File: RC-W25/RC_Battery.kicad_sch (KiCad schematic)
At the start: 18 parts, among them P2 CONN HEADER SMD R/A 2POS 2MM, SW3 SW_DPDT_x2, U2 AP62300TWU, U5 MCP73831-5-OT

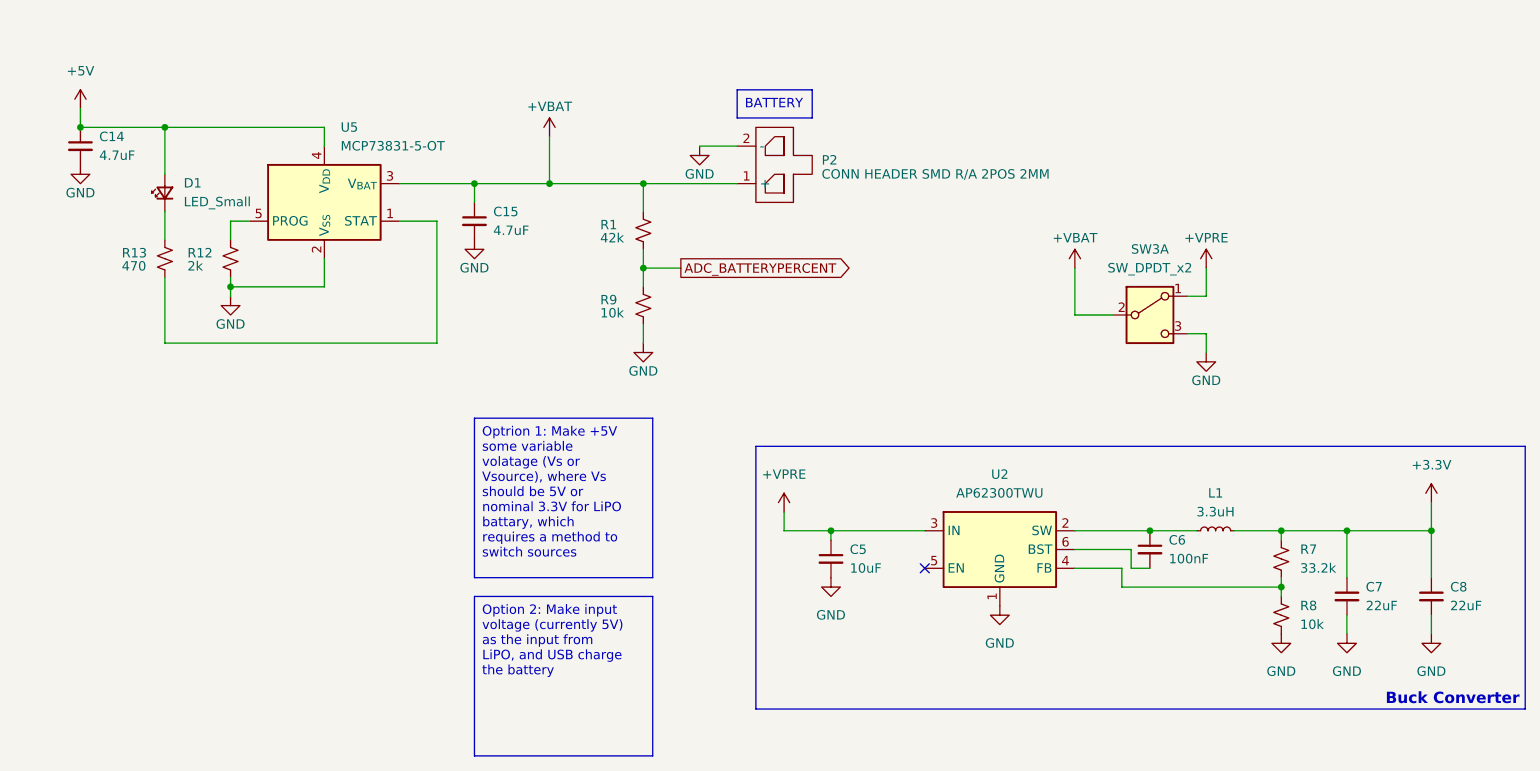
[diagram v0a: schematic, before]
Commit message: Updated Battery
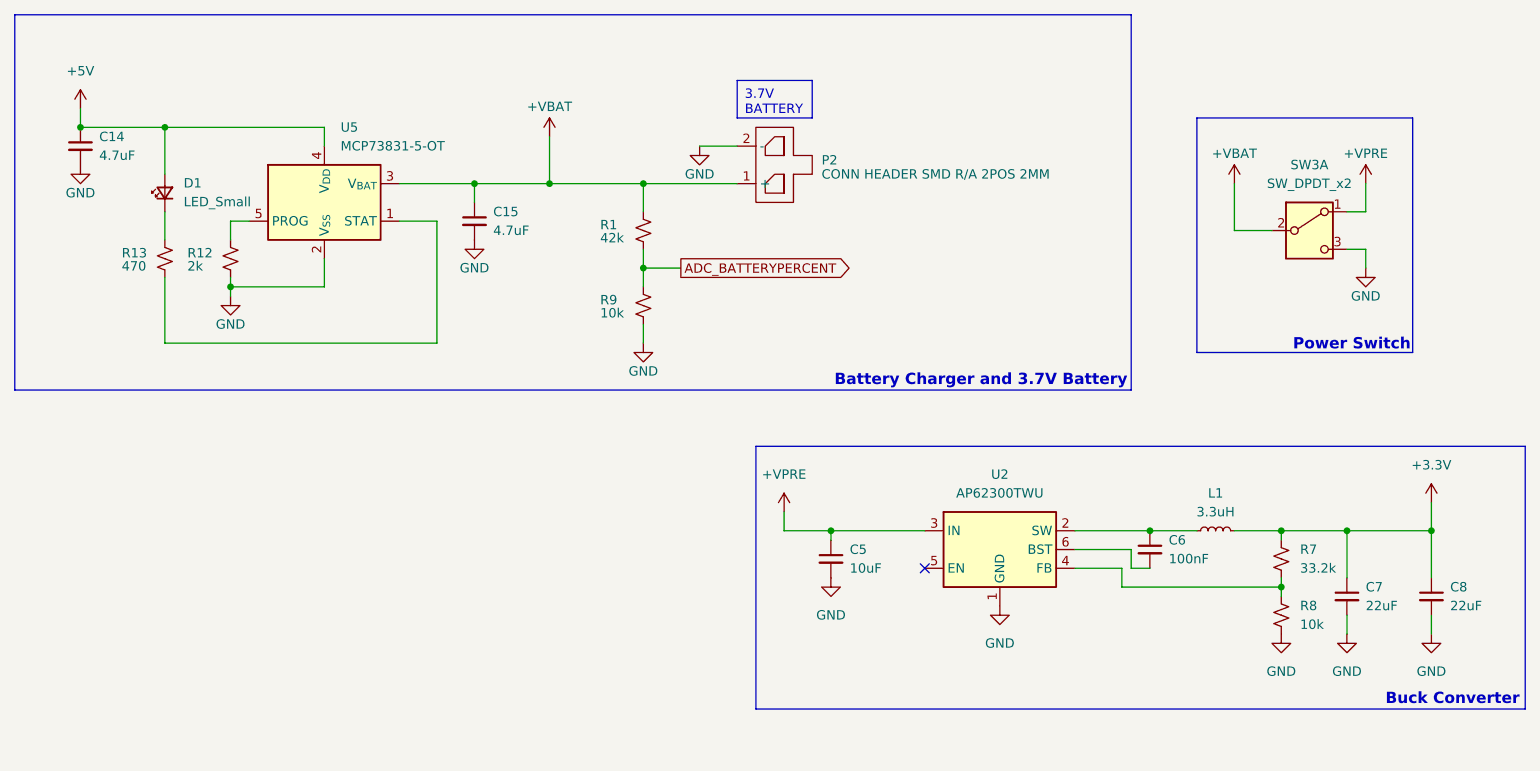
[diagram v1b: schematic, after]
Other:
- note added: "Battery Charger and 3.7V Battery"
- note added: "Power Switch"
- moved on the sheet: SW3A
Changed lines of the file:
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@@
 	(wire
 		(pts
-			(xy 204.47 81.28) (xy 204.47 85.09)
+			(xy 226.06 69.85) (xy 226.06 73.66)
 		)
 		(stroke
@@
 	(wire
 		(pts
-			(xy 186.69 81.28) (xy 186.69 87.63)
+			(xy 208.28 69.85) (xy 208.28 76.2)
 		)
 		(stroke
@@
 	(wire
 		(pts
-			(xy 204.47 92.71) (xy 204.47 90.17)
+			(xy 226.06 81.28) (xy 226.06 78.74)
 		)
 		(stroke
@@
 	(wire
 		(pts
-			(xy 201.93 85.09) (xy 204.47 85.09)
-		)
-		(stroke
-			(width 0)
-			(type default)
-		)
-	)
-	(wire
-		(pts
-			(xy 186.69 87.63) (xy 191.77 87.63)
+			(xy 223.52 73.66) (xy 226.06 73.66)
+		)
+		(stroke
+			(width 0)
+			(type default)
+		)
+	)
+	(wire
+		(pts
+			(xy 208.28 76.2) (xy 213.36 76.2)
 		)
 		(stroke
@@
 	(wire
 		(pts
-			(xy 204.47 90.17) (xy 201.93 90.17)
+			(xy 226.06 78.74) (xy 223.52 78.74)
 		)
 		(stroke
@@
 		)
 	)
-	(text_box "Option 2: Make input voltage (currently 5V) as the input from LiPO, and USB charge the battery"
-		(exclude_from_sim no)
-		(at 105.41 125.73 0)
-		(size 24.13 21.59)
+	(rectangle
+		(start 203.2 60.96)
+		(end 232.41 92.71)
 		(stroke
 			(width 0)
@@
 			(type none)
 		)
-		(effects
-			(font
-				(size 1.27 1.27)
-			)
-			(justify left top)
-		)
-	)
-	(text_box "Optrion 1: Make +5V some variable volatage (Vs or Vsource), where Vs should be 5V or nominal 3.3V for LiPO battary, which requires a method to switch sources"
-		(exclude_from_sim no)
-		(at 105.41 101.6 0)
-		(size 24.13 21.59)
+	)
+	(rectangle
+		(start 43.18 46.99)
+		(end 194.31 97.79)
 		(stroke
 			(width 0)
@@
 			(type none)
 		)
-		(effects
-			(font
-				(size 1.27 1.27)
-			)
-			(justify left top)
-		)
-	)
-	(text_box "BATTERY\n"
-		(exclude_from_sim no)
-		(at 140.97 57.15 0)
-		(size 10.16 3.81)
+	)
+	(text_box "3.7V BATTERY\n"
+		(exclude_from_sim no)
+		(at 140.97 55.88 0)
+		(size 10.16 5.08)
 		(stroke
 			(width 0)
@@
 		)
 	)
+	(text "Battery Charger and 3.7V Battery"
+		(exclude_from_sim no)
+		(at 193.802 96.52 0)
+		(effects
+			(font
+				(face "KiCad Font")
+				(size 1.524 1.524)
+				(thickness 0.3048)
+				(bold yes)
+			)
+			(justify right)
+		)
+	)
+	(text "Power Switch\n"
+		(exclude_from_sim no)
+		(at 232.156 91.694 0)
+		(effects
+			(font
+				(face "KiCad Font")
+				(size 1.524 1.524)
+				(thickness 0.3048)
+				(bold yes)
+			)
+			(justify right)
+		)
+	)
 	(global_label "ADC_BATTERYPERCENT"
 		(shape output)
@@
 	(symbol
 		(lib_id "power:+5V")
-		(at 186.69 81.28 0)
+		(at 208.28 69.85 0)
 		(unit 1)
 		(exclude_from_sim no)
@@
 		(dnp no)
 		(property "Reference" "#PWR042"
-			(at 186.69 85.09 0)
+			(at 208.28 73.66 0)
 			(effects
 				(font
@@
 		)
 		(property "Value" "+VBAT"
-			(at 186.69 77.216 0)
+			(at 208.28 65.786 0)
 			(effects
 				(font
@@
 		)
 		(property "Footprint" ""
-			(at 186.69 81.28 0)
+			(at 208.28 69.85 0)
 			(effects
 				(font
@@
 		)
 		(property "Datasheet" ""
-			(at 186.69 81.28 0)
+			(at 208.28 69.85 0)
 			(effects
 				(font
@@
 		)
 		(property "Description" "Power symbol creates a global label with name \"+5V\""
-			(at 186.69 81.28 0)
+			(at 208.28 69.85 0)
 			(effects
 				(font
@@
 	(symbol
 		(lib_id "Switch:SW_DPDT_x2")
-		(at 196.85 87.63 0)
+		(at 218.44 76.2 0)
 		(unit 1)
 		(exclude_from_sim no)
@@
 		(fields_autoplaced yes)
 		(property "Reference" "SW3"
-			(at 196.85 78.74 0)
+			(at 218.44 67.31 0)
 			(effects
 				(font
@@
 		)
 		(property "Value" "SW_DPDT_x2"
-			(at 196.85 81.28 0)
+			(at 218.44 69.85 0)
 			(effects
 				(font
@@
 		)
 		(property "Footprint" ""
-			(at 196.85 87.63 0)
+			(at 218.44 76.2 0)
 			(effects
 				(font
@@
 		)
 		(property "Datasheet" "~"
-			(at 196.85 87.63 0)
+			(at 218.44 76.2 0)
 			(effects
 				(font
@@
 		)
 		(property "Description" "Switch, dual pole double throw, separate symbols"
-			(at 196.85 87.63 0)
+			(at 218.44 76.2 0)
 			(effects
 				(font
@@
 	(symbol
 		(lib_id "power:GND")
-		(at 204.47 92.71 0)
+		(at 226.06 81.28 0)
 		(unit 1)
 		(exclude_from_sim no)
@@
 		(dnp no)
 		(property "Reference" "#PWR041"
-			(at 204.47 99.06 0)
+			(at 226.06 87.63 0)
 			(effects
 				(font
@@
 		)
 		(property "Value" "GND"
-			(at 204.47 96.52 0)
+			(at 226.06 85.09 0)
 			(effects
 				(font
@@
 		)
 		(property "Footprint" ""
-			(at 204.47 92.71 0)
+			(at 226.06 81.28 0)
 			(effects
 				(font
@@
 		)
 		(property "Datasheet" ""
-			(at 204.47 92.71 0)
+			(at 226.06 81.28 0)
 			(effects
 				(font
@@
 		)
 		(property "Description" "Power symbol creates a global label with name \"GND\" , ground"
-			(at 204.47 92.71 0)
+			(at 226.06 81.28 0)
 			(effects
 				(font
@@
 	(symbol
 		(lib_id "power:+5V")
-		(at 204.47 81.28 0)
+		(at 226.06 69.85 0)
 		(unit 1)
 		(exclude_from_sim no)
@@
 		(dnp no)
 		(property "Reference" "#PWR043"
-			(at 204.47 85.09 0)
+			(at 226.06 73.66 0)
 			(effects
 				(font
@@
 		)
 		(property "Value" "+VPRE"
-			(at 204.47 77.216 0)
+			(at 226.06 65.786 0)
 			(effects
 				(font
@@
 		)
 		(property "Footprint" ""
-			(at 204.47 81.28 0)
+			(at 226.06 69.85 0)
 			(effects
 				(font
@@
 		)
 		(property "Datasheet" ""
-			(at 204.47 81.28 0)
+			(at 226.06 69.85 0)
 			(effects
 				(font
@@
 		)
 		(property "Description" "Power symbol creates a global label with name \"+5V\""
-			(at 204.47 81.28 0)
-			(effects
-				(font
+			(at 226.06 69.85 0)
+			(effects
+				(font

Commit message: fixed resistors
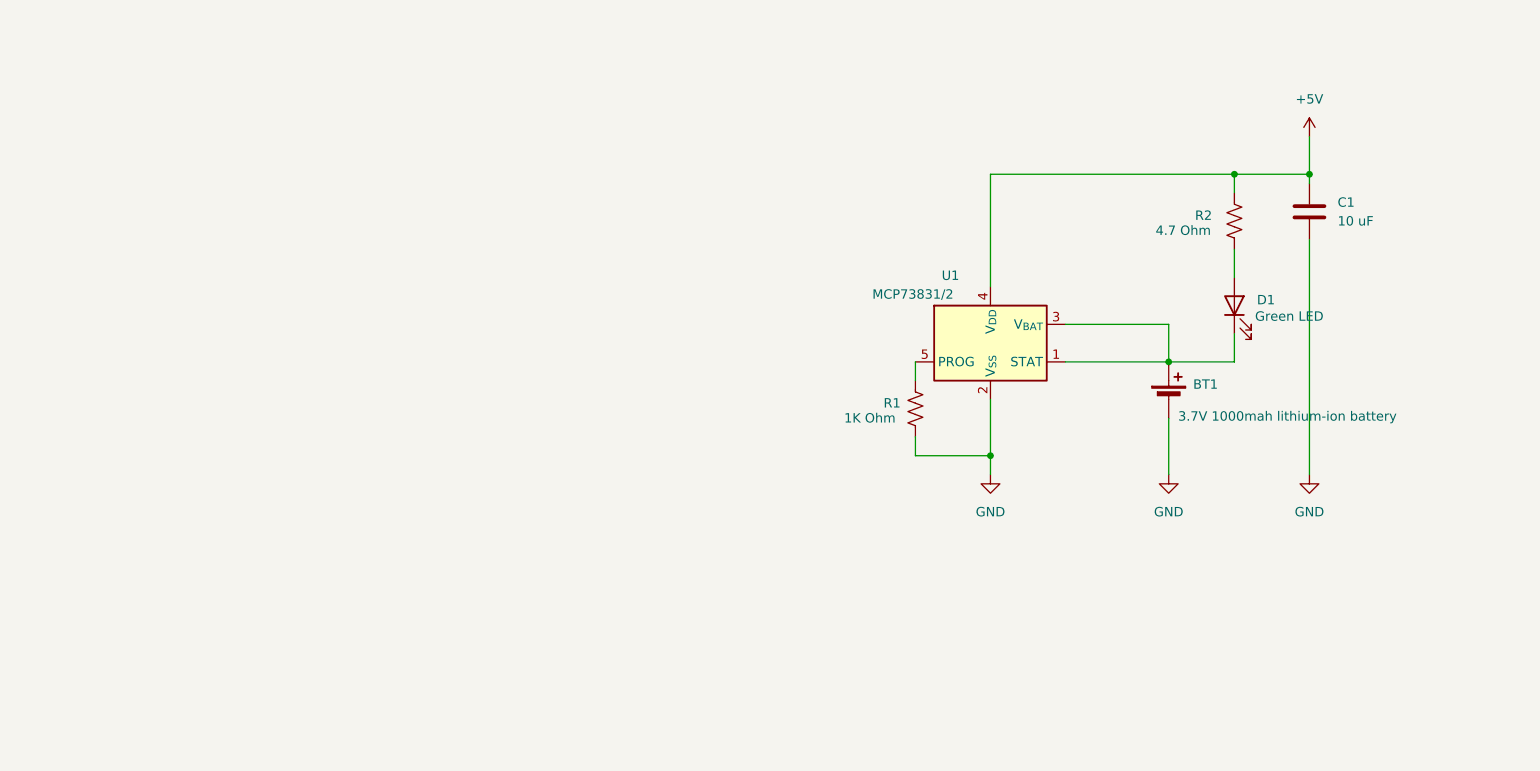
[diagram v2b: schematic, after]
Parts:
- removed C14, C15: 4.7uF, Capacitor_SMD:C_0603_1608Metric, symbol Device:C_Small
- removed C5: 10uF, Capacitor_SMD:C_0603_1608Metric, symbol Device:C_Small
- removed C6: 100nF, Capacitor_SMD:C_0603_1608Metric, symbol Device:C_Small
- removed C7, C8: 22uF, Capacitor_SMD:C_0603_1608Metric, symbol Device:C_Small
- removed D1: LED_Small, symbol Device:LED_Small
- removed L1: 3.3uH, symbol Device:L_Small
- removed P2: CONN HEADER SMD R/A 2POS 2MM, symbol New_Library:DuraClik_CONN_HEADER_SMD_R/A_2POS_2MM
- removed R1: 42k, Resistor_SMD:R_0603_1608Metric, symbol Device:R_Small_US
- removed R12: 2k, Resistor_SMD:R_0603_1608Metric, symbol Device:R_Small_US
- removed R13: 470, Resistor_SMD:R_0603_1608Metric, symbol Device:R_Small_US
- removed R7: 33.2k, Resistor_SMD:R_0603_1608Metric, symbol Device:R_Small_US
- removed R8, R9: 10k, Resistor_SMD:R_0603_1608Metric, symbol Device:R_Small_US
- removed SW3: SW_DPDT_x2, symbol Switch:SW_DPDT_x2
- removed U2: AP62300TWU, Package_TO_SOT_SMD:TSOT-23-6, symbol Regulator_Switching:AP62300TWU
- removed U5: MCP73831-5-OT, Package_TO_SOT_SMD:SOT-23-5, symbol Battery_Management:MCP73831-5-OT
- added BT1: 3.7V 1000mah lithium-ion battery, symbol Device:Battery_Cell
- added C1: 10 uF, Capacitor_SMD:C_0402_1005Metric, symbol Device:C
- added D1: Green LED, LED_SMD:LED_0402_1005Metric, symbol Device:LED
- added R1: 1K Ohm, Resistor_SMD:R_0402_1005Metric, symbol Device:R_US
- added R2: 4.7 Ohm, Resistor_SMD:R_0402_1005Metric, symbol Device:R_US
- added U1: MCP73831/2, Package_TO_SOT_SMD:SOT-23-5, symbol Battery_Management:MCP73831-2-OT
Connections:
- net +5V: now also C1.1, R2.1, U1.4 (V_{DD})
- net GND: now also BT1.2 (-), C1.2, R1.2, U1.2 (V_{SS})
- new net: BT1.1 (+), D1.1 (K), U1.1 (STAT), U1.3 (V_{BAT})
- new net: D1.2 (A), R2.2
- new net: R1.1, U1.5 (PROG)
- no-connect marks 1 -> 0
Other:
- note removed: "Battery Charger and 3.7V Battery"
- note removed: "Buck Converter"
- note removed: "Power Switch"
